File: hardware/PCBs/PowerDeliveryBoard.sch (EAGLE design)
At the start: 13 parts, among them IC1 7812T, IC2 7812T, J1 XT60-M, J3 T2M-105-01-X-D-TH, U1 GENERIC-SOIC8MSGEQ7N-FILTER

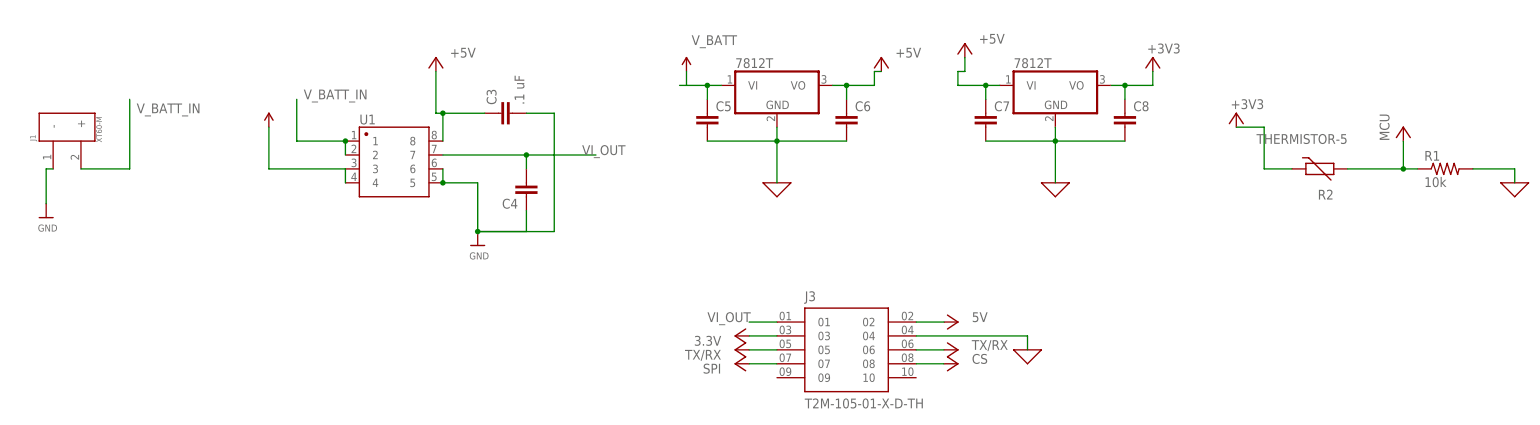
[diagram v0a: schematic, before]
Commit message: Add Power Board | Change MB Connector Pins | Move Old PDB.sch to PCBs Folder
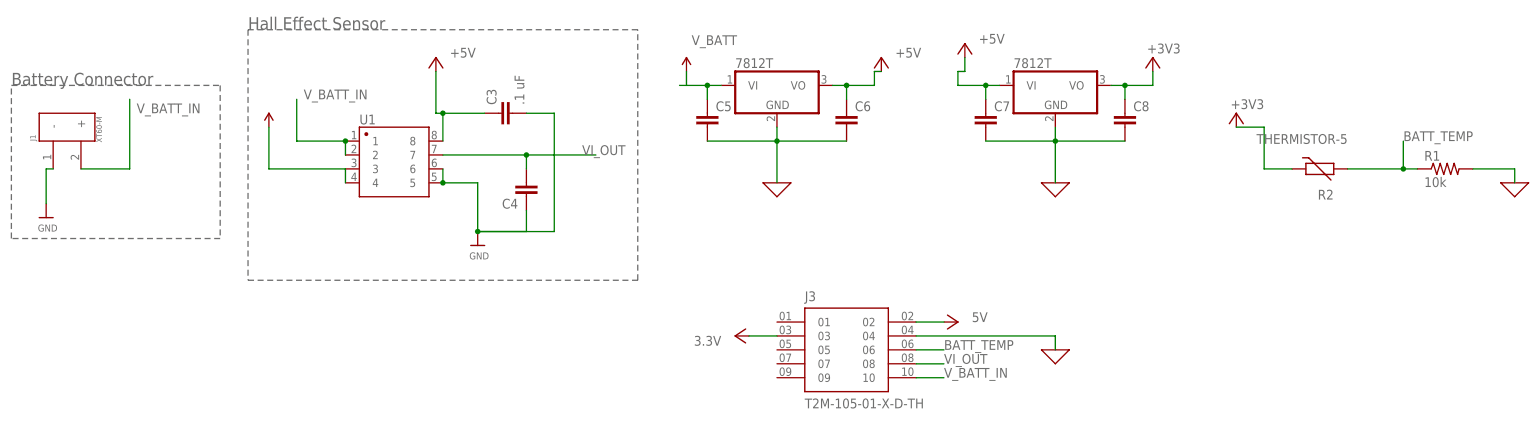
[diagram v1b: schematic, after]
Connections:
- new net BATT_TEMP: J3.06, R1.1, R2.2
- net VCC: no longer J3.05, J3.06, J3.07, J3.08, R1.1, R2.2
- net VI_OUT: now also J3.08; no longer J3.01
- net V_BATT_IN: now also J3.10
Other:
- note added: "Battery Connector"
- note added: "Hall Effect Sensor"
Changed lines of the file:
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@@
 <?xml version="1.0" encoding="utf-8"?>
 <!DOCTYPE eagle SYSTEM "eagle.dtd">
-<eagle version="9.5.1">
+<eagle version="9.6.2">
 <drawing>
 <settings>
@@
 <schematic_group name="3.3VREGULATOR"/>
 <schematic_group name="THERMISTOR"/>
-<schematic_group name="CONNECTOR"/>
+<schematic_group name="SAMTEC_CONNECTOR"/>
 </groups>
 <parts>
@@
 <part name="C8" library="capacitor-wima" library_urn="urn:adsk.eagle:library:116" deviceset="C" device="2,5-3" package3d_urn="urn:adsk.eagle:package:5436/1"/>
 <part name="X_5" library="ngspice-simulation" library_urn="urn:adsk.eagle:library:527439" deviceset="GND" device=""/>
-<part name="P+9" library="supply1" library_urn="urn:adsk.eagle:library:371" deviceset="VCC" device="" value="MCU"/>
 <part name="R2" library="varistor" library_urn="urn:adsk.eagle:library:410" deviceset="THERMISTOR" device="-5" package3d_urn="urn:adsk.eagle:package:30591/1"/>
 <part name="IC1" library="linear" library_urn="urn:adsk.eagle:library:262" deviceset="78*" device="T" package3d_urn="urn:adsk.eagle:package:16414/1" technology="12"/>
@@
 <part name="P+13" library="supply1" library_urn="urn:adsk.eagle:library:371" deviceset="VCC" device="" value="3.3V"/>
 <part name="X_6" library="ngspice-simulation" library_urn="urn:adsk.eagle:library:527439" deviceset="GND" device=""/>
-<part name="P+14" library="supply1" library_urn="urn:adsk.eagle:library:371" deviceset="VCC" device="" value="TX/RX"/>
-<part name="P+15" library="supply1" library_urn="urn:adsk.eagle:library:371" deviceset="VCC" device="" value="CS"/>
-<part name="P+16" library="supply1" library_urn="urn:adsk.eagle:library:371" deviceset="VCC" device="" value="TX/RX"/>
-<part name="P+17" library="supply1" library_urn="urn:adsk.eagle:library:371" deviceset="VCC" device="" value="SPI"/>
 <part name="U1" library="SparkFun-Retired" deviceset="GENERIC-SOIC8" device="MSGEQ7N-FILTER"/>
 <part name="J1" library="XT60-M" library_urn="urn:adsk.eagle:library:23078652" deviceset="XT60-M" device="" package3d_urn="urn:adsk.eagle:package:23078655/1"/>
@@
 <sheet>
 <plain>
+<wire x1="53.34" y1="33.02" x2="-17.78" y2="33.02" width="0.1524" layer="95" style="shortdash"/>
+<wire x1="-17.78" y1="33.02" x2="-17.78" y2="-12.7" width="0.1524" layer="95" style="shortdash"/>
+<wire x1="-17.78" y1="-12.7" x2="53.34" y2="-12.7" width="0.1524" layer="95" style="shortdash"/>
+<wire x1="53.34" y1="-12.7" x2="53.34" y2="33.02" width="0.1524" layer="95" style="shortdash"/>
+<wire x1="-22.86" y1="22.86" x2="-22.86" y2="-5.08" width="0.1524" layer="95" style="shortdash"/>
+<wire x1="-22.86" y1="-5.08" x2="-60.96" y2="-5.08" width="0.1524" layer="95" style="shortdash"/>
+<wire x1="-60.96" y1="-5.08" x2="-60.96" y2="22.86" width="0.1524" layer="95" style="shortdash"/>
+<wire x1="-60.96" y1="22.86" x2="-22.86" y2="22.86" width="0.1524" layer="95" style="shortdash"/>
+<text x="-60.96" y="22.86" size="2.286" layer="95">Battery Connector</text>
+<text x="-17.78" y="33.02" size="2.286" layer="95">Hall Effect Sensor</text>
 </plain>
 <instances>
@@
 </instance>
 <instance part="X_5" gate="G$1" x="213.36" y="5.08" smashed="yes" grouprefs="THERMISTOR"/>
-<instance part="P+9" gate="VCC" x="193.04" y="15.24" smashed="yes" grouprefs="THERMISTOR">
-<attribute name="VALUE" x="190.5" y="12.7" size="1.778" layer="96" rot="R90"/>
-</instance>
 <instance part="R2" gate="G$1" x="177.8" y="7.62" smashed="yes" rot="R180" grouprefs="THERMISTOR">
 <attribute name="NAME" x="180.34" y="3.81" size="1.778" layer="95" rot="R180"/>
@@
 <attribute name="VALUE" x="196.85" y="4.318" size="1.778" layer="96"/>
 </instance>
-<instance part="J3" gate="G$1" x="91.44" y="-25.4" smashed="yes" grouprefs="CONNECTOR">
+<instance part="J3" gate="G$1" x="91.44" y="-25.4" smashed="yes" grouprefs="SAMTEC_CONNECTOR">
 <attribute name="NAME" x="83.82" y="-16.51" size="1.778" layer="95"/>
 <attribute name="VALUE" x="83.82" y="-34.29" size="1.778" layer="96" align="top-left"/>
 </instance>
-<instance part="P+12" gate="VCC" x="111.76" y="-20.32" smashed="yes" rot="R270" grouprefs="CONNECTOR">
+<instance part="P+12" gate="VCC" x="111.76" y="-20.32" smashed="yes" rot="R270" grouprefs="SAMTEC_CONNECTOR">
 <attribute name="VALUE" x="114.3" y="-20.32" size="1.778" layer="96"/>
 </instance>
-<instance part="P+13" gate="VCC" x="71.12" y="-22.86" smashed="yes" rot="R90" grouprefs="CONNECTOR">
+<instance part="P+13" gate="VCC" x="71.12" y="-22.86" smashed="yes" rot="R90" grouprefs="SAMTEC_CONNECTOR">
 <attribute name="VALUE" x="68.58" y="-22.86" size="1.778" layer="96" rot="R180"/>
 </instance>
-<instance part="X_6" gate="G$1" x="124.46" y="-25.4" smashed="yes" grouprefs="CONNECTOR"/>
-<instance part="P+14" gate="VCC" x="111.76" y="-25.4" smashed="yes" rot="R270" grouprefs="CONNECTOR">
-<attribute name="VALUE" x="114.3" y="-25.4" size="1.778" layer="96"/>
-</instance>
-<instance part="P+15" gate="VCC" x="111.76" y="-27.94" smashed="yes" rot="R270" grouprefs="CONNECTOR">
-<attribute name="VALUE" x="114.3" y="-27.94" size="1.778" layer="96"/>
-</instance>
-<instance part="P+16" gate="VCC" x="71.12" y="-25.4" smashed="yes" rot="R90" grouprefs="CONNECTOR">
-<attribute name="VALUE" x="68.58" y="-25.4" size="1.778" layer="96" rot="R180"/>
-</instance>
-<instance part="P+17" gate="VCC" x="71.12" y="-27.94" smashed="yes" rot="R90" grouprefs="CONNECTOR">
-<attribute name="VALUE" x="68.58" y="-27.94" size="1.778" layer="96" rot="R180"/>
-</instance>
+<instance part="X_6" gate="G$1" x="129.54" y="-25.4" smashed="yes" grouprefs="SAMTEC_CONNECTOR"/>
 <instance part="U1" gate="G$1" x="2.54" y="12.7" smashed="yes">
 <attribute name="NAME" x="2.54" y="15.748" size="1.778" layer="95"/>
@@
 <segment>
 <pinref part="J3" gate="G$1" pin="04"/>
-<wire x1="104.14" y1="-22.86" x2="124.46" y2="-22.86" width="0.1524" layer="91" grouprefs="CONNECTOR"/>
-<wire x1="124.46" y1="-22.86" x2="124.46" y2="-25.4" width="0.1524" layer="91" grouprefs="CONNECTOR"/>
+<wire x1="104.14" y1="-22.86" x2="129.54" y2="-22.86" width="0.1524" layer="91" grouprefs="SAMTEC_CONNECTOR"/>
+<wire x1="129.54" y1="-22.86" x2="129.54" y2="-25.4" width="0.1524" layer="91" grouprefs="SAMTEC_CONNECTOR"/>
 <pinref part="X_6" gate="G$1" pin="0"/>
 </segment>
@@
 <net name="VCC" class="0">
 <segment>
-<wire x1="193.04" y1="7.62" x2="195.58" y2="7.62" width="0.1524" layer="91" grouprefs="THERMISTOR"/>
-<pinref part="P+9" gate="VCC" pin="VCC"/>
-<wire x1="193.04" y1="12.7" x2="193.04" y2="7.62" width="0.1524" layer="91" grouprefs="THERMISTOR"/>
-<pinref part="R2" gate="G$1" pin="2"/>
-<wire x1="182.88" y1="7.62" x2="193.04" y2="7.62" width="0.1524" layer="91" grouprefs="THERMISTOR"/>
-<junction x="193.04" y="7.62" grouprefs="THERMISTOR"/>
-<pinref part="R1" gate="G$1" pin="1"/>
-</segment>
-<segment>
 <pinref part="J3" gate="G$1" pin="02"/>
-<wire x1="104.14" y1="-20.32" x2="109.22" y2="-20.32" width="0.1524" layer="91" grouprefs="CONNECTOR"/>
+<wire x1="104.14" y1="-20.32" x2="109.22" y2="-20.32" width="0.1524" layer="91" grouprefs="SAMTEC_CONNECTOR"/>
 <pinref part="P+12" gate="VCC" pin="VCC"/>
 </segment>
 <segment>
 <pinref part="J3" gate="G$1" pin="03"/>
-<wire x1="78.74" y1="-22.86" x2="73.66" y2="-22.86" width="0.1524" layer="91" grouprefs="CONNECTOR"/>
+<wire x1="78.74" y1="-22.86" x2="73.66" y2="-22.86" width="0.1524" layer="91" grouprefs="SAMTEC_CONNECTOR"/>
 <pinref part="P+13" gate="VCC" pin="VCC"/>
-</segment>
-<segment>
-<pinref part="J3" gate="G$1" pin="06"/>
-<wire x1="104.14" y1="-25.4" x2="109.22" y2="-25.4" width="0.1524" layer="91" grouprefs="CONNECTOR"/>
-<pinref part="P+14" gate="VCC" pin="VCC"/>
-</segment>
-<segment>
-<pinref part="J3" gate="G$1" pin="08"/>
-<wire x1="104.14" y1="-27.94" x2="109.22" y2="-27.94" width="0.1524" layer="91" grouprefs="CONNECTOR"/>
-<pinref part="P+15" gate="VCC" pin="VCC"/>
-</segment>
-<segment>
-<pinref part="P+16" gate="VCC" pin="VCC"/>
-<pinref part="J3" gate="G$1" pin="05"/>
-<wire x1="73.66" y1="-25.4" x2="78.74" y2="-25.4" width="0.1524" layer="91" grouprefs="CONNECTOR"/>
-</segment>
-<segment>
-<pinref part="J3" gate="G$1" pin="07"/>
-<pinref part="P+17" gate="VCC" pin="VCC"/>
-<wire x1="78.74" y1="-27.94" x2="73.66" y2="-27.94" width="0.1524" layer="91" grouprefs="CONNECTOR"/>
 </segment>
 </net>
@@
 <label x="-38.1" y="17.78" size="1.778" layer="95"/>
 </segment>
+<segment>
+<pinref part="J3" gate="G$1" pin="10"/>
+<wire x1="104.14" y1="-30.48" x2="109.22" y2="-30.48" width="0.1524" layer="91"/>
+<label x="109.22" y="-30.48" size="1.778" layer="95"/>
+</segment>
 </net>
 <net name="VI_OUT" class="0">
@@
 </segment>
 <segment>
-<pinref part="J3" gate="G$1" pin="01"/>
-<wire x1="78.74" y1="-20.32" x2="73.66" y2="-20.32" width="0.1524" layer="91" grouprefs="CONNECTOR"/>
-<label x="66.04" y="-20.32" size="1.778" layer="95"/>
-</segment>
-</net>
+<pinref part="J3" gate="G$1" pin="08"/>
+<wire x1="104.14" y1="-27.94" x2="109.22" y2="-27.94" width="0.1524" layer="91"/>
+<label x="109.22" y="-27.94" size="1.778" layer="95"/>
+</segment>
+</net>
+<net name="BATT_TEMP" class="0">
+<segment>
+<wire x1="193.04" y1="7.62" x2="195.58" y2="7.62" width="0.1524" layer="91" grouprefs="THERMISTOR"/>
+<wire x1="193.04" y1="12.7" x2="193.04" y2="7.62" width="0.1524" layer="91" grouprefs="THERMISTOR"/>
+<pinref part="R2" gate="G$1" pin="2"/>
+<wire x1="182.88" y1="7.62" x2="193.04" y2="7.62" width="0.1524" layer="91" grouprefs="THERMISTOR"/>
+<junction x="193.04" y="7.62" grouprefs="THERMISTOR"/>
+<pinref part="R1" gate="G$1" pin="1"/>
+<label x="193.04" y="12.7" size="1.778" layer="95"/>
+</segment>
+<segment>
+<pinref part="J3" gate="G$1" pin="06"/>
+<wire x1="104.14" y1="-25.4" x2="109.22" y2="-25.4" width="0.1524" layer="91"/>
+<label x="109.22" y="-25.4" size="1.778" layer="95"/>
+</segment>
+</net>
